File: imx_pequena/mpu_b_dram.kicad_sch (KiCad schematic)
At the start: 4 parts, among them U1 MCIMX6Z0DVM09AB, U2 MT41K64M16TW-107:J_TR

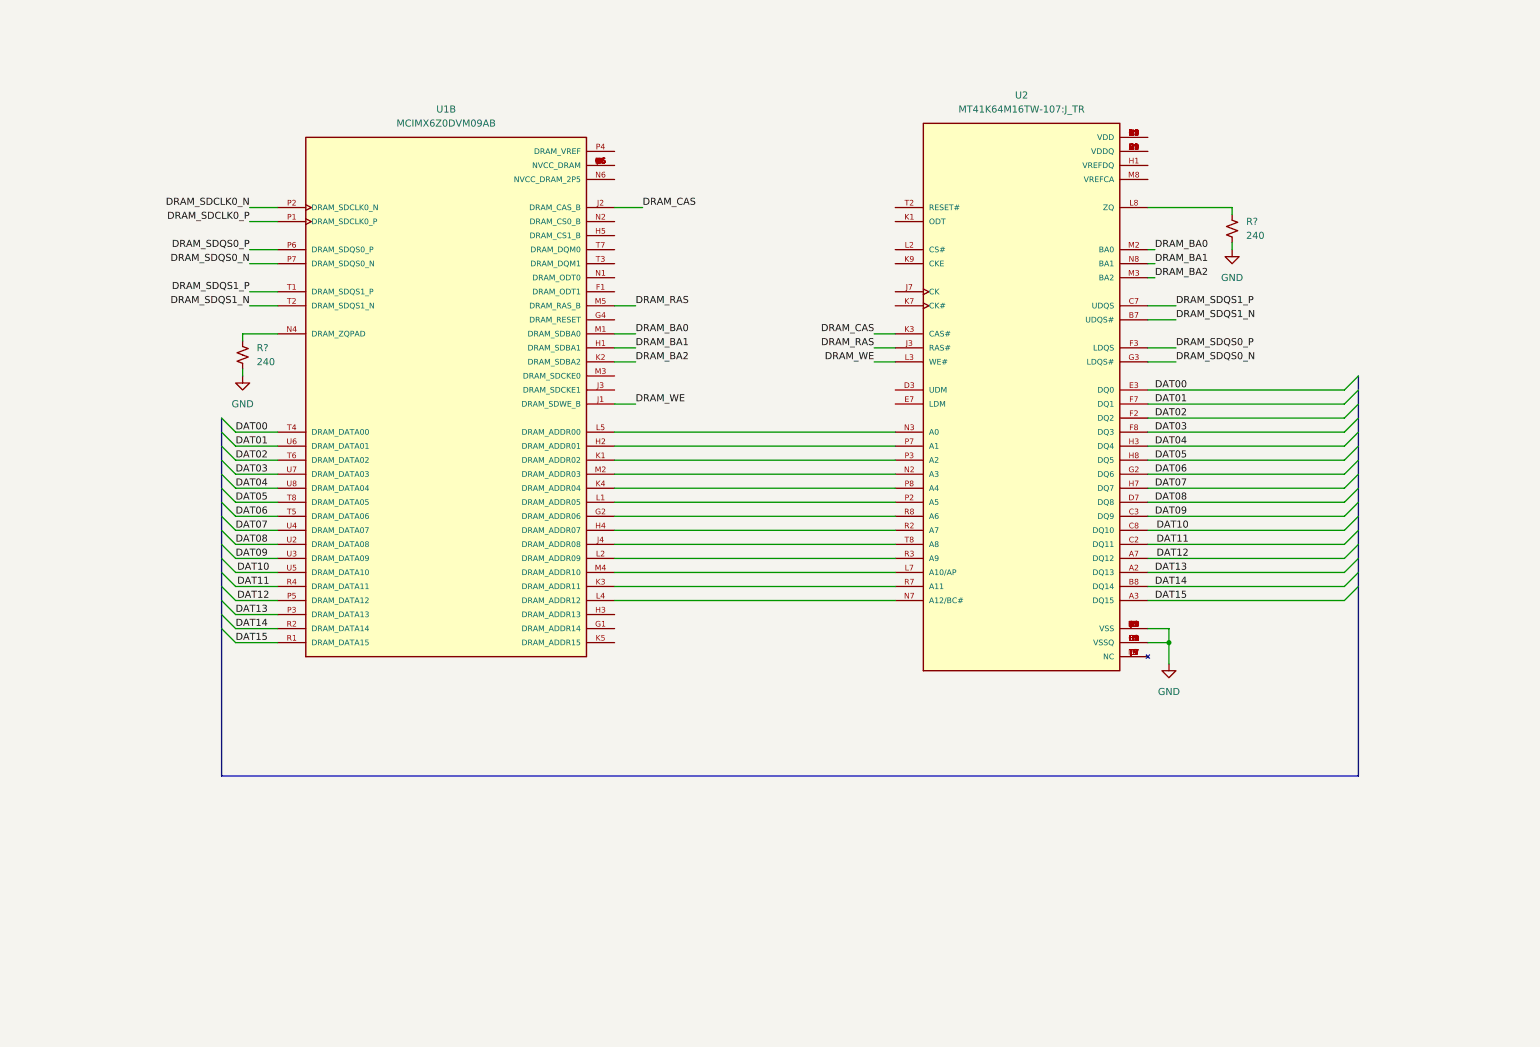
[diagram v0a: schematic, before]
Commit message: Updated DRAM
DRAM Schematic tentatively done
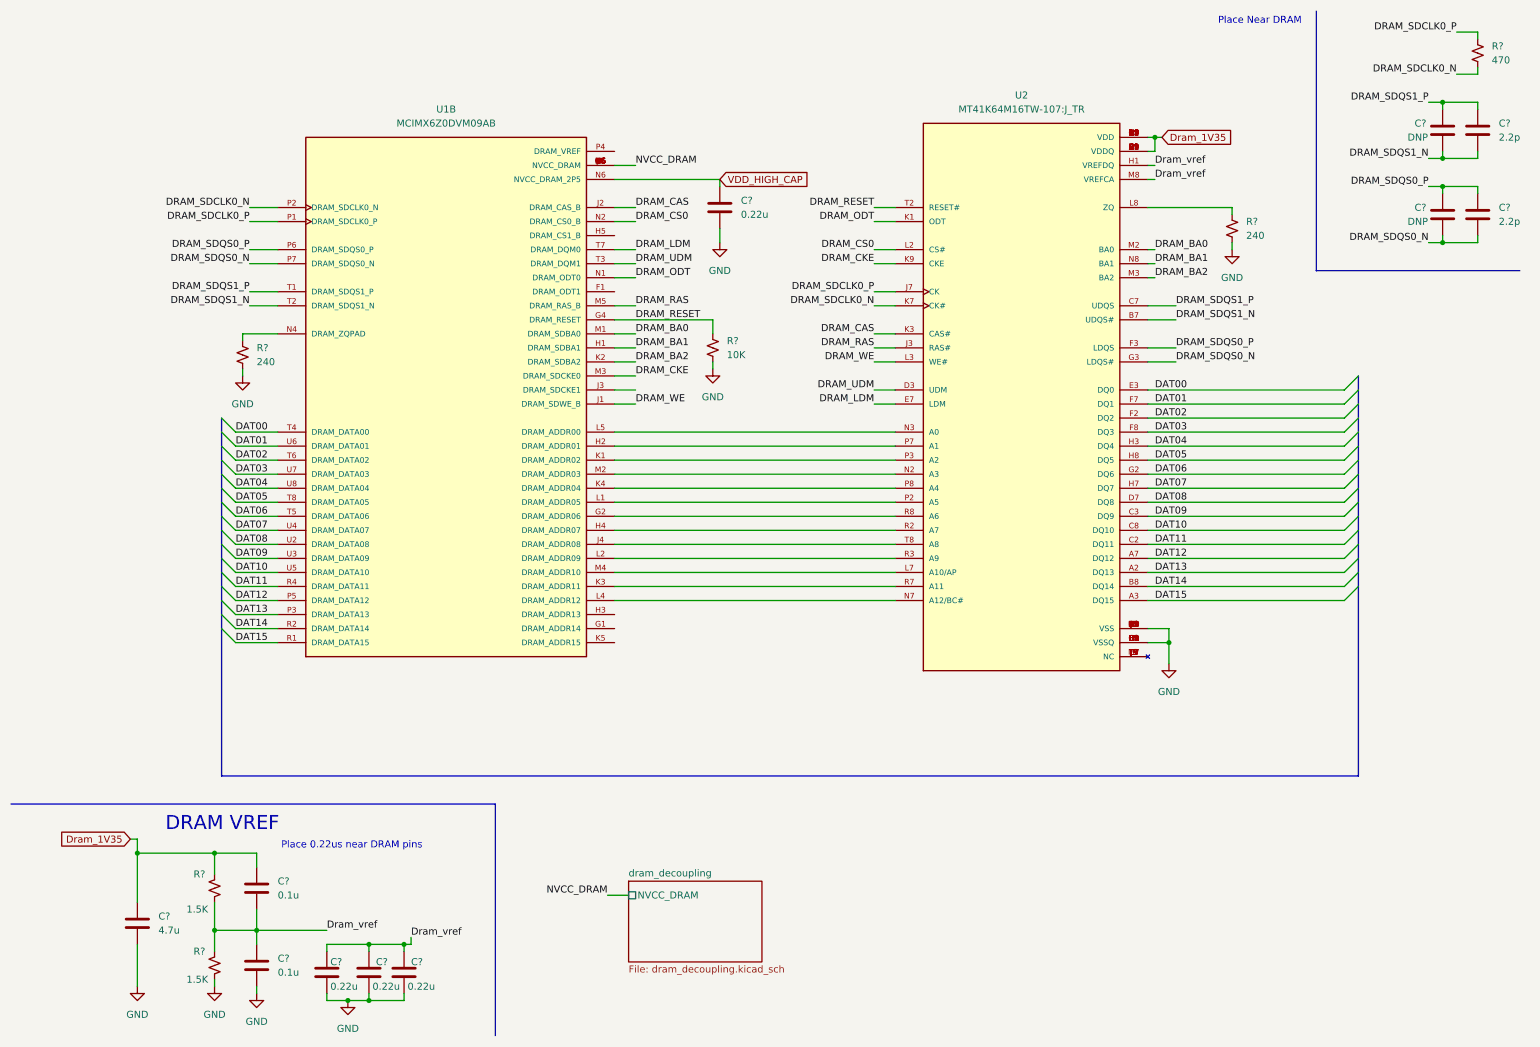
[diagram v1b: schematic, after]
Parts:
- added C? (x2): 2.2p, symbol Device:C
- added C? (x4): 0.22u, symbol Device:C
- added C? (x2): 0.1u, symbol Device:C
- added C? (x2): DNP, symbol Device:C
- added C?: 4.7u, symbol Device:C
- added R?: 470, symbol Device:R_Small_US
- added R?: 10K, symbol Device:R_Small_US
- added R? (x2): 1.5K, symbol Device:R_Small_US
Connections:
- net DRAM_SDCLK0_N: now also U2.K7 (CK#), R?.2
- net DRAM_SDCLK0_P: now also U2.J7 (CK), R?.1
- net DRAM_SDQS0_N: now also C?.2, C?.2
- net DRAM_SDQS0_P: now also C?.1, C?.1
- net DRAM_SDQS1_N: now also C?.2, C?.2
- net DRAM_SDQS1_P: now also C?.1, C?.1
- net GND: now also C?.2, C?.2, C?.2, C?.2, C?.2, C?.2, R?.2, R?.2
- net DRAM_RESET: now reaches U1.G4 (DRAM_RESET)
- net DRAM_RESET: now also U2.T2 (RESET#), R?.1
- net NVCC_DRAM: now reaches U1.G6 (NVCC_DRAM), U1.H6 (NVCC_DRAM), U1.J6 (NVCC_DRAM), U1.K6 (NVCC_DRAM), U1.L6 (NVCC_DRAM), U1.M6 (NVCC_DRAM)
- net DRAM_CKE: now reaches U1.M3 (DRAM_SDCKE0)
- net DRAM_CKE: now also U2.K9 (CKE)
- net DRAM_ODT: now reaches U1.N1 (DRAM_ODT0)
- net DRAM_ODT: now also U2.K1 (ODT)
- net DRAM_CS0: now reaches U1.N2 (DRAM_CS0_B)
- net DRAM_CS0: now also U2.L2 (CS#)
- net VDD_HIGH_CAP: now reaches U1.N6 (NVCC_DRAM_2P5)
- net VDD_HIGH_CAP: now also C?.1
- net DRAM_UDM: now reaches U1.T3 (DRAM_DQM1)
- net DRAM_UDM: now also U2.D3 (UDM)
- net DRAM_LDM: now reaches U1.T7 (DRAM_DQM0)
- net DRAM_LDM: now also U2.E7 (LDM)
- net Dram_1V35: now reaches U2.A1 (VDDQ), U2.A8 (VDDQ), U2.C1 (VDDQ), U2.C9 (VDDQ), U2.D2 (VDDQ), U2.E9 (VDDQ), U2.F1 (VDDQ), U2.H2 (VDDQ), U2.H9 (VDDQ)
- net Dram_1V35: now also U2.B2 (VDD), U2.D9 (VDD), U2.G7 (VDD), U2.K2 (VDD), U2.K8 (VDD), U2.N1 (VDD), U2.N9 (VDD), U2.R1 (VDD), U2.R9 (VDD), C?.1, C?.1, R?.1
- net Dram_vref: now reaches U2.H1 (VREFDQ)
- net Dram_vref: now also U2.M8 (VREFCA), C?.1, C?.1, C?.1, C?.1, C?.2, R?.1, R?.2
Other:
- added sheet dram_decoupling (dram_decoupling.kicad_sch)
- note added: "DRAM VREF"
- note added: "Place 0.22us near DRAM pins"
- note added: "Place Near DRAM"

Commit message: SD card + pinot files
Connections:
- net Dram_vref: now also U1.P4 (DRAM_VREF)
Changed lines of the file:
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@@
+    (stroke (width 0) (type default) (color 0 0 0 0))
+  )
+  (wire (pts (xy 120.65 38.1) (xy 124.46 38.1))
     (stroke (width 0) (type default) (color 0 0 0 0))
   )
@@
     (effects (font (size 1.27 1.27)) (justify right bottom))
   )
+  (label "Dram_vref" (at 124.46 38.1 0)
+    (effects (font (size 1.27 1.27)) (justify left bottom))
+  )
   (label "DAT09" (at 52.07 111.76 0)

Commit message: Power Update
Added 3v3 and 1.35V switchers
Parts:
- gave numbers to parts that had none: 17
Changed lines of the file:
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@@
   (symbol (lib_id "power:GND") (at 220.98 130.81 0) (unit 1)
     (in_bom yes) (on_board yes) (fields_autoplaced)
-    (property "Reference" "#PWR?" (id 0) (at 220.98 137.16 0)
+    (property "Reference" "#PWR0114" (id 0) (at 220.98 137.16 0)
       (effects (font (size 1.27 1.27)) hide)
     )
@@
   (symbol (lib_id "power:GND") (at 55.88 190.5 0) (unit 1)
     (in_bom yes) (on_board yes) (fields_autoplaced)
-    (property "Reference" "#PWR?" (id 0) (at 55.88 196.85 0)
+    (property "Reference" "#PWR0112" (id 0) (at 55.88 196.85 0)
       (effects (font (size 1.27 1.27)) hide)
     )
@@
   (symbol (lib_id "Device:C") (at 276.86 34.29 0) (unit 1)
     (in_bom yes) (on_board yes) (fields_autoplaced)
-    (property "Reference" "C?" (id 0) (at 280.67 33.0199 0)
+    (property "Reference" "C16" (id 0) (at 280.67 33.0199 0)
       (effects (font (size 1.27 1.27)) (justify left))
     )
@@
   (symbol (lib_id "power:GND") (at 232.41 55.88 0) (unit 1)
     (in_bom yes) (on_board yes) (fields_autoplaced)
-    (property "Reference" "#PWR?" (id 0) (at 232.41 62.23 0)
+    (property "Reference" "#PWR0115" (id 0) (at 232.41 62.23 0)
       (effects (font (size 1.27 1.27)) hide)
     )
@@
   (symbol (lib_id "Device:C") (at 139.7 48.26 0) (unit 1)
     (in_bom yes) (on_board yes) (fields_autoplaced)
-    (property "Reference" "C?" (id 0) (at 143.51 46.9899 0)
+    (property "Reference" "C13" (id 0) (at 143.51 46.9899 0)
       (effects (font (size 1.27 1.27)) (justify left))
     )
@@
   (symbol (lib_id "Device:R_Small_US") (at 276.86 20.32 0) (unit 1)
     (in_bom yes) (on_board yes) (fields_autoplaced)
-    (property "Reference" "R?" (id 0) (at 279.4 19.0499 0)
+    (property "Reference" "R8" (id 0) (at 279.4 19.0499 0)
       (effects (font (size 1.27 1.27)) (justify left))
     )
@@
   (symbol (lib_id "Device:R_Small_US") (at 138.43 73.66 0) (unit 1)
     (in_bom yes) (on_board yes) (fields_autoplaced)
-    (property "Reference" "R?" (id 0) (at 140.97 72.3899 0)
+    (property "Reference" "R6" (id 0) (at 140.97 72.3899 0)
       (effects (font (size 1.27 1.27)) (justify left))
     )
@@
   (symbol (lib_id "Device:R_Small_US") (at 48.26 185.42 0) (mirror y) (unit 1)
     (in_bom yes) (on_board yes)
-    (property "Reference" "R?" (id 0) (at 44.45 182.88 0)
+    (property "Reference" "R4" (id 0) (at 44.45 182.88 0)
       (effects (font (size 1.27 1.27)) (justify right))
     )
@@
   (symbol (lib_id "power:GND") (at 48.26 189.23 0) (unit 1)
     (in_bom yes) (on_board yes) (fields_autoplaced)
-    (property "Reference" "#PWR?" (id 0) (at 48.26 195.58 0)
+    (property "Reference" "#PWR0113" (id 0) (at 48.26 195.58 0)
       (effects (font (size 1.27 1.27)) hide)
     )
@@
   (symbol (lib_id "Device:C") (at 82.55 186.69 0) (unit 1)
     (in_bom yes) (on_board yes)
-    (property "Reference" "C?" (id 0) (at 83.82 184.785 0)
+    (property "Reference" "C12" (id 0) (at 83.82 184.785 0)
       (effects (font (size 1.27 1.27)) (justify left))
     )
@@
   (symbol (lib_id "power:GND") (at 138.43 77.47 0) (unit 1)
     (in_bom yes) (on_board yes) (fields_autoplaced)
-    (property "Reference" "#PWR?" (id 0) (at 138.43 83.82 0)
+    (property "Reference" "#PWR0109" (id 0) (at 138.43 83.82 0)
       (effects (font (size 1.27 1.27)) hide)
     )
@@
   (symbol (lib_id "power:GND") (at 53.34 78.74 0) (unit 1)
     (in_bom yes) (on_board yes) (fields_autoplaced)
-    (property "Reference" "#PWR?" (id 0) (at 53.34 85.09 0)
+    (property "Reference" "#PWR0110" (id 0) (at 53.34 85.09 0)
       (effects (font (size 1.27 1.27)) hide)
     )
@@
   (symbol (lib_id "Device:C") (at 55.88 171.45 0) (unit 1)
     (in_bom yes) (on_board yes) (fields_autoplaced)
-    (property "Reference" "C?" (id 0) (at 59.69 170.1799 0)
+    (property "Reference" "C8" (id 0) (at 59.69 170.1799 0)
       (effects (font (size 1.27 1.27)) (justify left))
     )
@@
   (symbol (lib_id "Device:C") (at 55.88 185.42 0) (unit 1)
     (in_bom yes) (on_board yes) (fields_autoplaced)
-    (property "Reference" "C?" (id 0) (at 59.69 184.1499 0)
+    (property "Reference" "C9" (id 0) (at 59.69 184.1499 0)
       (effects (font (size 1.27 1.27)) (justify left))
     )
@@
   (symbol (lib_id "power:GND") (at 34.29 189.23 0) (unit 1)
     (in_bom yes) (on_board yes) (fields_autoplaced)
-    (property "Reference" "#PWR?" (id 0) (at 34.29 195.58 0)
+    (property "Reference" "#PWR0107" (id 0) (at 34.29 195.58 0)
       (effects (font (size 1.27 1.27)) hide)
     )
@@
   (symbol (lib_id "Device:C") (at 270.51 34.29 0) (unit 1)
     (in_bom yes) (on_board yes)
-    (property "Reference" "C?" (id 0) (at 265.43 33.02 0)
+    (property "Reference" "C14" (id 0) (at 265.43 33.02 0)
       (effects (font (size 1.27 1.27)) (justify left))
     )
@@
   (symbol (lib_id "power:GND") (at 139.7 54.61 0) (unit 1)
     (in_bom yes) (on_board yes) (fields_autoplaced)
-    (property "Reference" "#PWR?" (id 0) (at 139.7 60.96 0)
+    (property "Reference" "#PWR0108" (id 0) (at 139.7 60.96 0)
       (effects (font (size 1.27 1.27)) hide)
     )
@@
   (symbol (lib_id "power:GND") (at 72.39 191.77 0) (unit 1)
     (in_bom yes) (on_board yes) (fields_autoplaced)
-    (property "Reference" "#PWR?" (id 0) (at 72.39 198.12 0)
+    (property "Reference" "#PWR0111" (id 0) (at 72.39 198.12 0)
       (effects (font (size 1.27 1.27)) hide)
     )
@@
   (symbol (lib_id "Device:R_Small_US") (at 232.41 52.07 0) (unit 1)
     (in_bom yes) (on_board yes) (fields_autoplaced)
-    (property "Reference" "R?" (id 0) (at 234.95 50.7999 0)
+    (property "Reference" "R7" (id 0) (at 234.95 50.7999 0)
       (effects (font (size 1.27 1.27)) (justify left))
     )
@@
   (symbol (lib_id "Device:C") (at 34.29 177.8 0) (unit 1)
     (in_bom yes) (on_board yes) (fields_autoplaced)
-    (property "Reference" "C?" (id 0) (at 38.1 176.5299 0)
+    (property "Reference" "C7" (id 0) (at 38.1 176.5299 0)
       (effects (font (size 1.27 1.27)) (justify left))
     )
@@
   (symbol (lib_id "Device:C") (at 68.58 186.69 0) (unit 1)
     (in_bom yes) (on_board yes)
-    (property "Reference" "C?" (id 0) (at 69.215 184.785 0)
+    (property "Reference" "C10" (id 0) (at 69.215 184.785 0)
       (effects (font (size 1.27 1.27)) (justify left))
     )
@@
   (symbol (lib_id "Device:R_Small_US") (at 48.26 171.45 0) (mirror y) (unit 1)
     (in_bom yes) (on_board yes)
-    (property "Reference" "R?" (id 0) (at 44.45 168.91 0)
+    (property "Reference" "R3" (id 0) (at 44.45 168.91 0)
       (effects (font (size 1.27 1.27)) (justify right))
     )
@@
   (symbol (lib_id "Device:R_Small_US") (at 53.34 74.93 0) (unit 1)
     (in_bom yes) (on_board yes) (fields_autoplaced)
-    (property "Reference" "R?" (id 0) (at 55.88 73.6599 0)
+    (property "Reference" "R5" (id 0) (at 55.88 73.6599 0)
       (effects (font (size 1.27 1.27)) (justify left))
     )
@@
   (symbol (lib_id "Device:C") (at 270.51 49.53 0) (unit 1)
     (in_bom yes) (on_board yes)
-    (property "Reference" "C?" (id 0) (at 265.43 48.26 0)
+    (property "Reference" "C15" (id 0) (at 265.43 48.26 0)
       (effects (font (size 1.27 1.27)) (justify left))
     )
@@
   (symbol (lib_id "Device:C") (at 76.2 186.69 0) (unit 1)
     (in_bom yes) (on_board yes)
-    (property "Reference" "C?" (id 0) (at 77.47 184.785 0)
+    (property "Reference" "C11" (id 0) (at 77.47 184.785 0)
       (effects (font (size 1.27 1.27)) (justify left))
     )
@@
   (symbol (lib_id "Device:C") (at 276.86 49.53 0) (unit 1)
     (in_bom yes) (on_board yes) (fields_autoplaced)
-    (property "Reference" "C?" (id 0) (at 280.67 48.2599 0)
-      (effects (font (size 1.27 1.27)) (justify left))
-    )
+    (property "Reference" "C17" (id 0) (at 280.67 48.2599 0)
+      (effects (font (size 1.27 1.27)) (justify left))
+    )

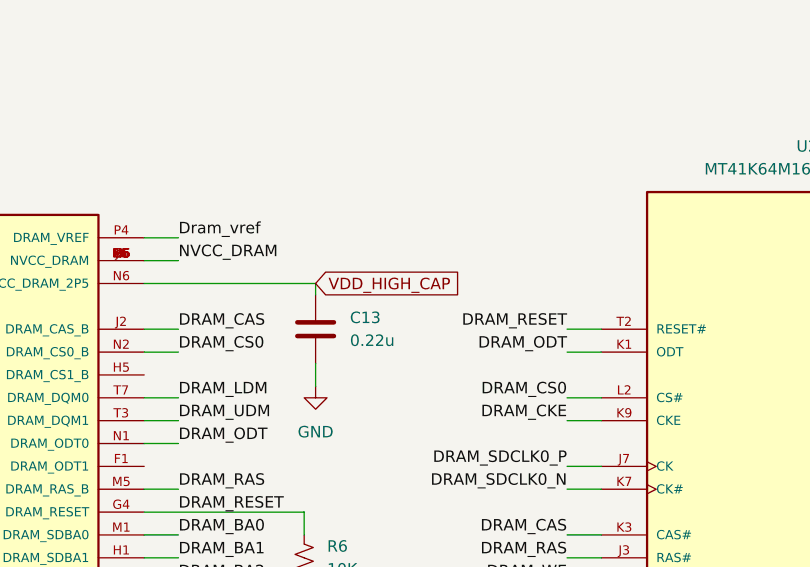
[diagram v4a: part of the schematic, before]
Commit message: Updated config
Updated config file and some pins
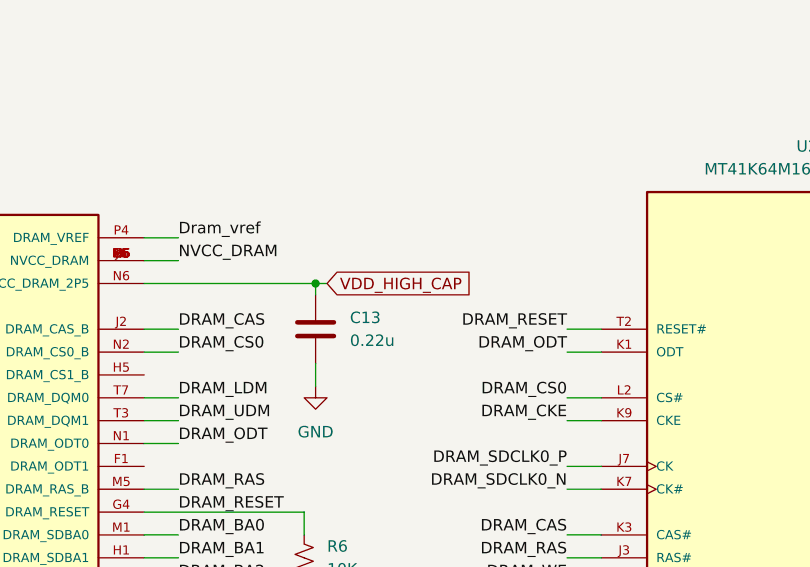
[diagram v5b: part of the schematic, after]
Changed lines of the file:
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@@
   (junction (at 34.29 165.1) (diameter 0) (color 0 0 0 0)
   )
+  (junction (at 139.7 43.18) (diameter 0) (color 0 0 0 0)
+  )
   (junction (at 270.51 44.45) (diameter 0) (color 0 0 0 0)
   )
@@
   )
   (wire (pts (xy 220.98 127) (xy 220.98 130.81))
+    (stroke (width 0) (type default) (color 0 0 0 0))
+  )
+  (wire (pts (xy 139.7 43.18) (xy 140.97 43.18))
     (stroke (width 0) (type default) (color 0 0 0 0))
   )
@@
     )
   )
-  (global_label "VDD_HIGH_CAP" (shape input) (at 139.7 43.18 0) (fields_autoplaced)
+  (global_label "VDD_HIGH_CAP" (shape input) (at 140.97 43.18 0) (fields_autoplaced)
     (effects (font (size 1.27 1.27)) (justify left))
-    (property "Intersheet References" "${INTERSHEET_REFS}" (id 0) (at 155.8412 43.1006 0)
+    (property "Intersheet References" "${INTERSHEET_REFS}" (id 0) (at 157.1112 43.1006 0)
       (effects (font (size 1.27 1.27)) (justify left) hide)
     )
